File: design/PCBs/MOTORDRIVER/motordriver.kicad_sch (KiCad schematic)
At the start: 0 parts

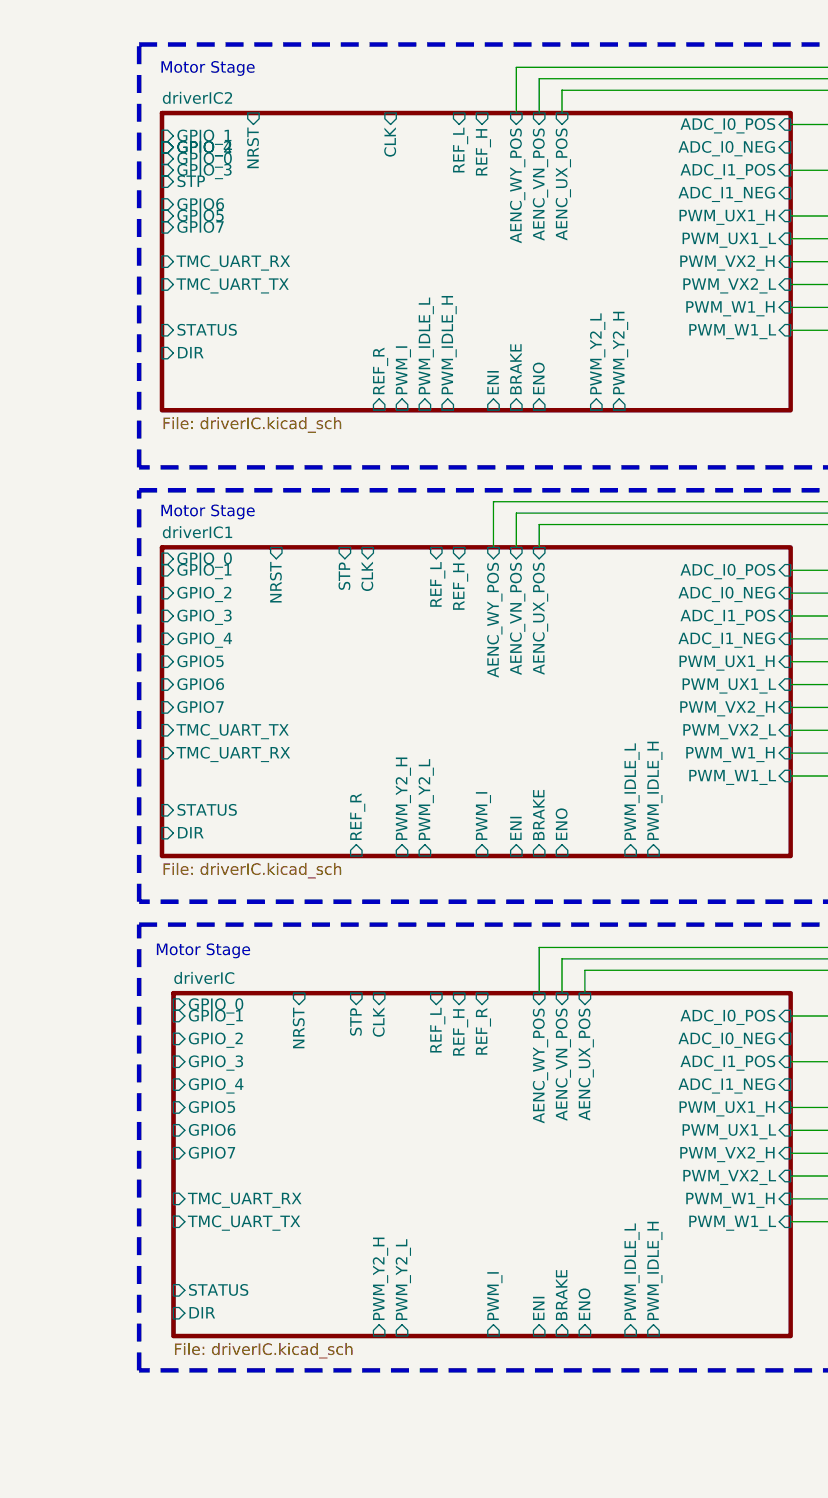
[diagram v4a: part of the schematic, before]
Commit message: Removed unneccessary TMC4761 pins
Finally went through every pin on the TMC and tried to eliminate
unneeded pins. Reduced sheet complexity quite nicely. Pretty much
all rationales for removing pins were added to the design document,
although not formatted that nicely yet.
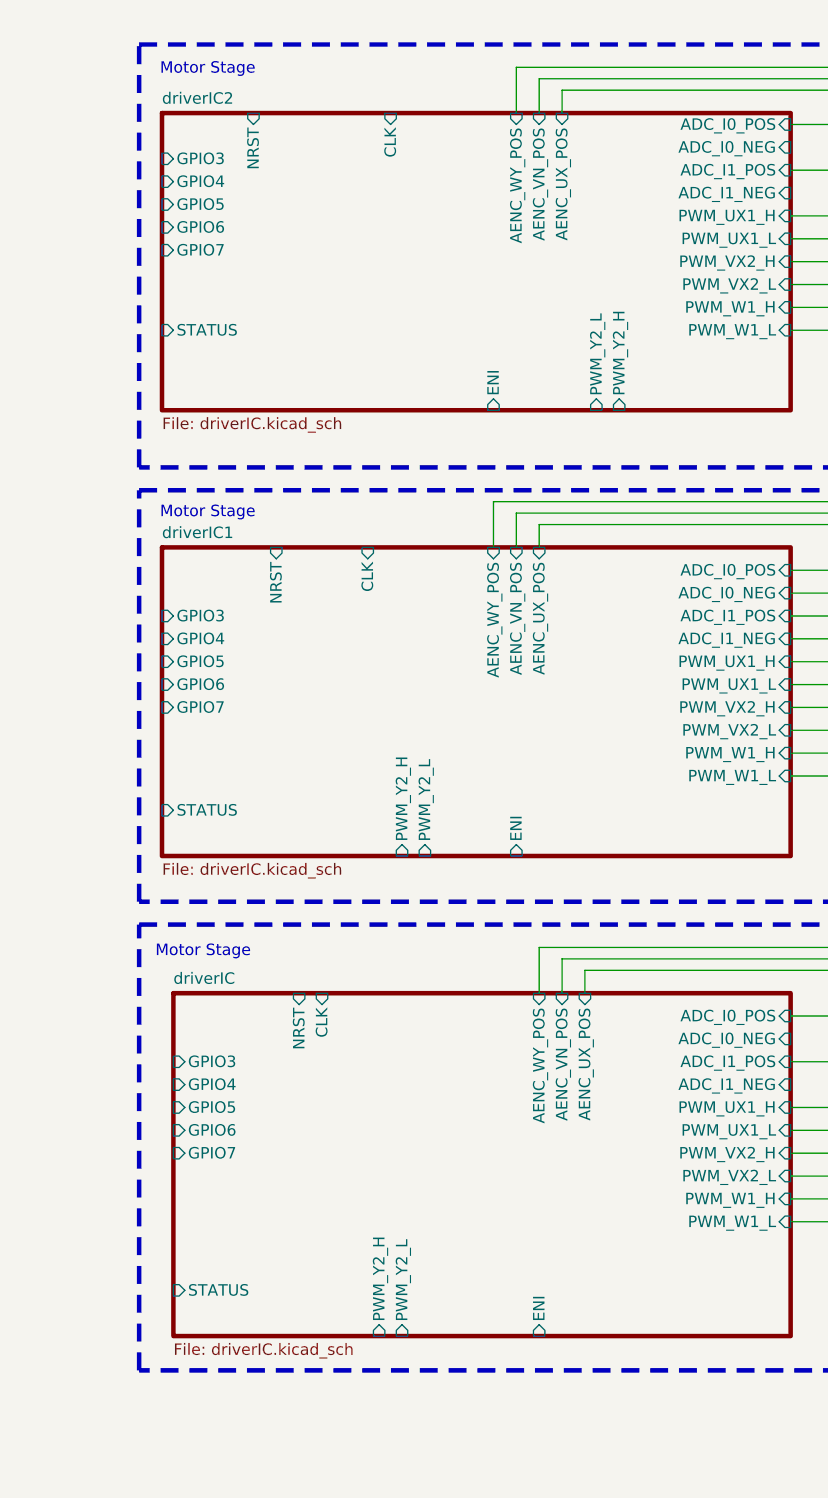
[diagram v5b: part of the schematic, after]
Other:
- sheet driverIC ports: added GPIO3, GPIO4; removed BRAKE, DIR, ENO, GPIO_0, GPIO_1, GPIO_2, GPIO_3, GPIO_4, PWM_I, PWM_IDLE_H, PWM_IDLE_L, REF_H, REF_L, REF_R, STP, TMC_UART_RX, TMC_UART_TX
- sheet driverIC1 ports: added GPIO3, GPIO4; removed BRAKE, DIR, ENO, GPIO_0, GPIO_1, GPIO_2, GPIO_3, GPIO_4, PWM_I, PWM_IDLE_H, PWM_IDLE_L, REF_H, REF_L, REF_R, STP, TMC_UART_RX, TMC_UART_TX
- sheet driverIC2 ports: added GPIO3, GPIO4; removed BRAKE, DIR, ENO, GPIO_0, GPIO_1, GPIO_2, GPIO_3, GPIO_4, PWM_I, PWM_IDLE_H, PWM_IDLE_L, REF_H, REF_L, REF_R, STP, TMC_UART_RX, TMC_UART_TX

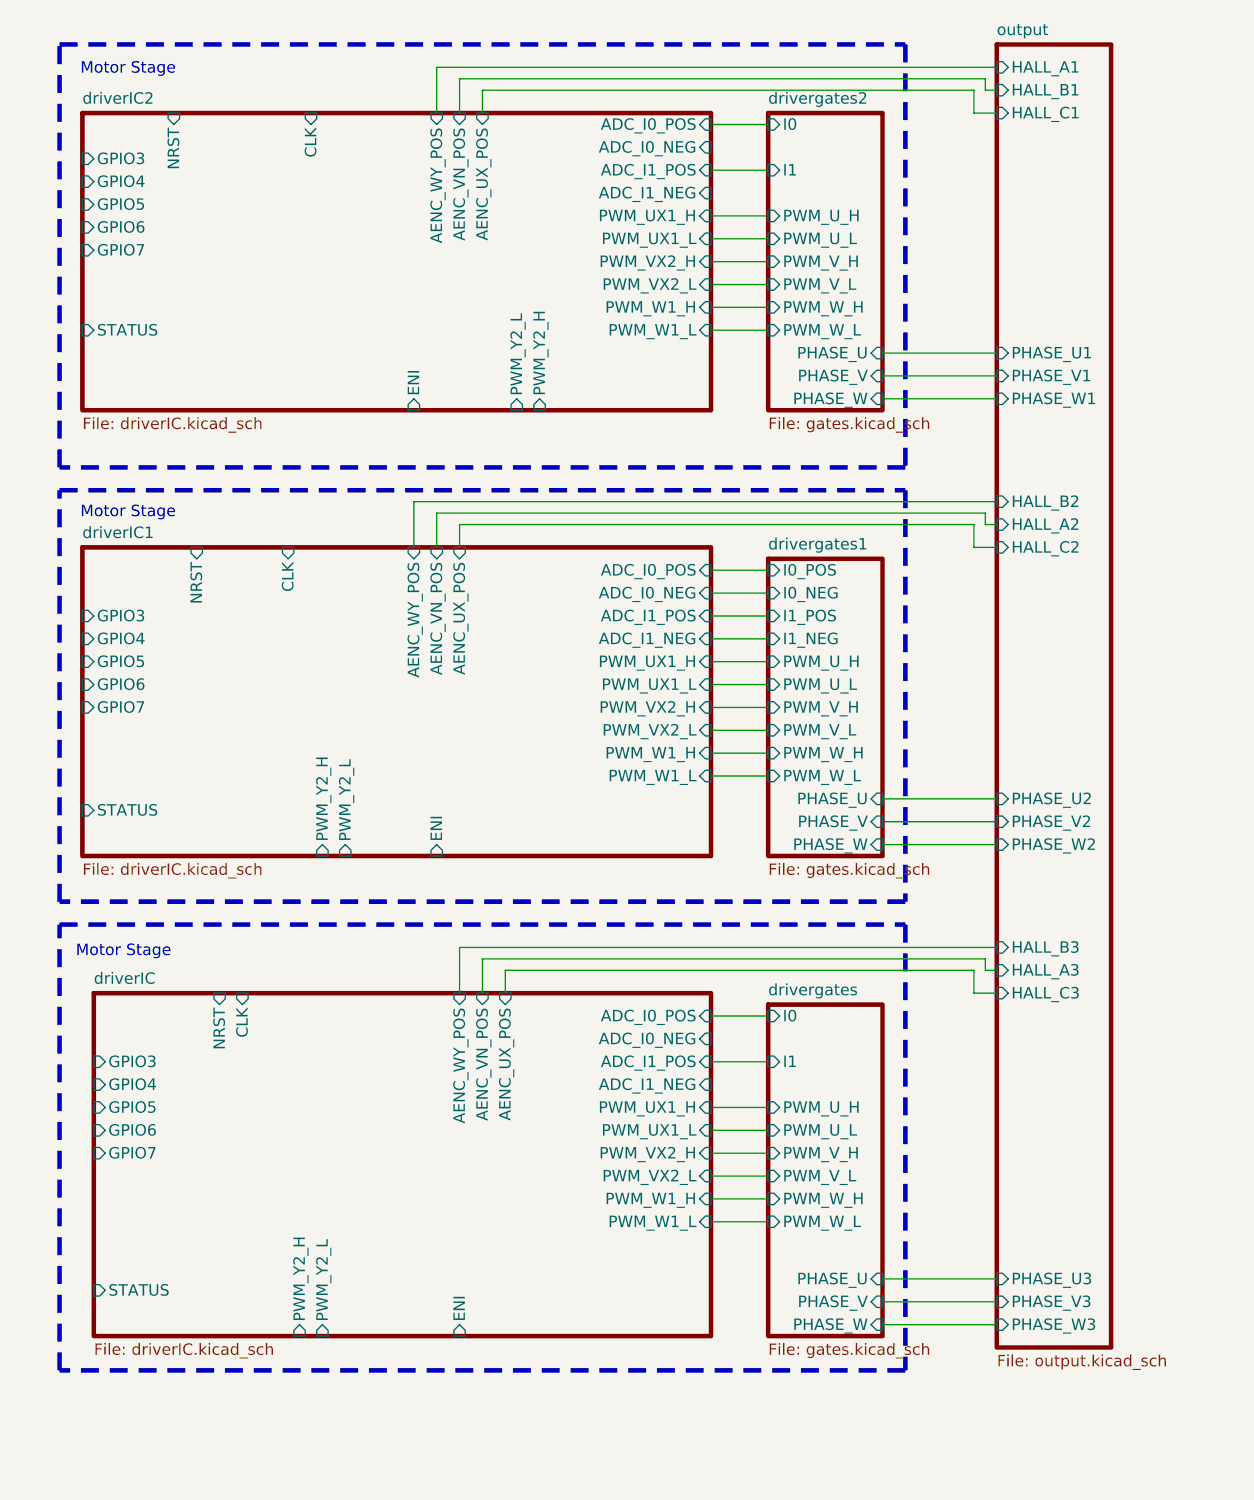
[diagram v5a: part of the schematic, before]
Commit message: Switched TMC hall sensor input to digital from motors
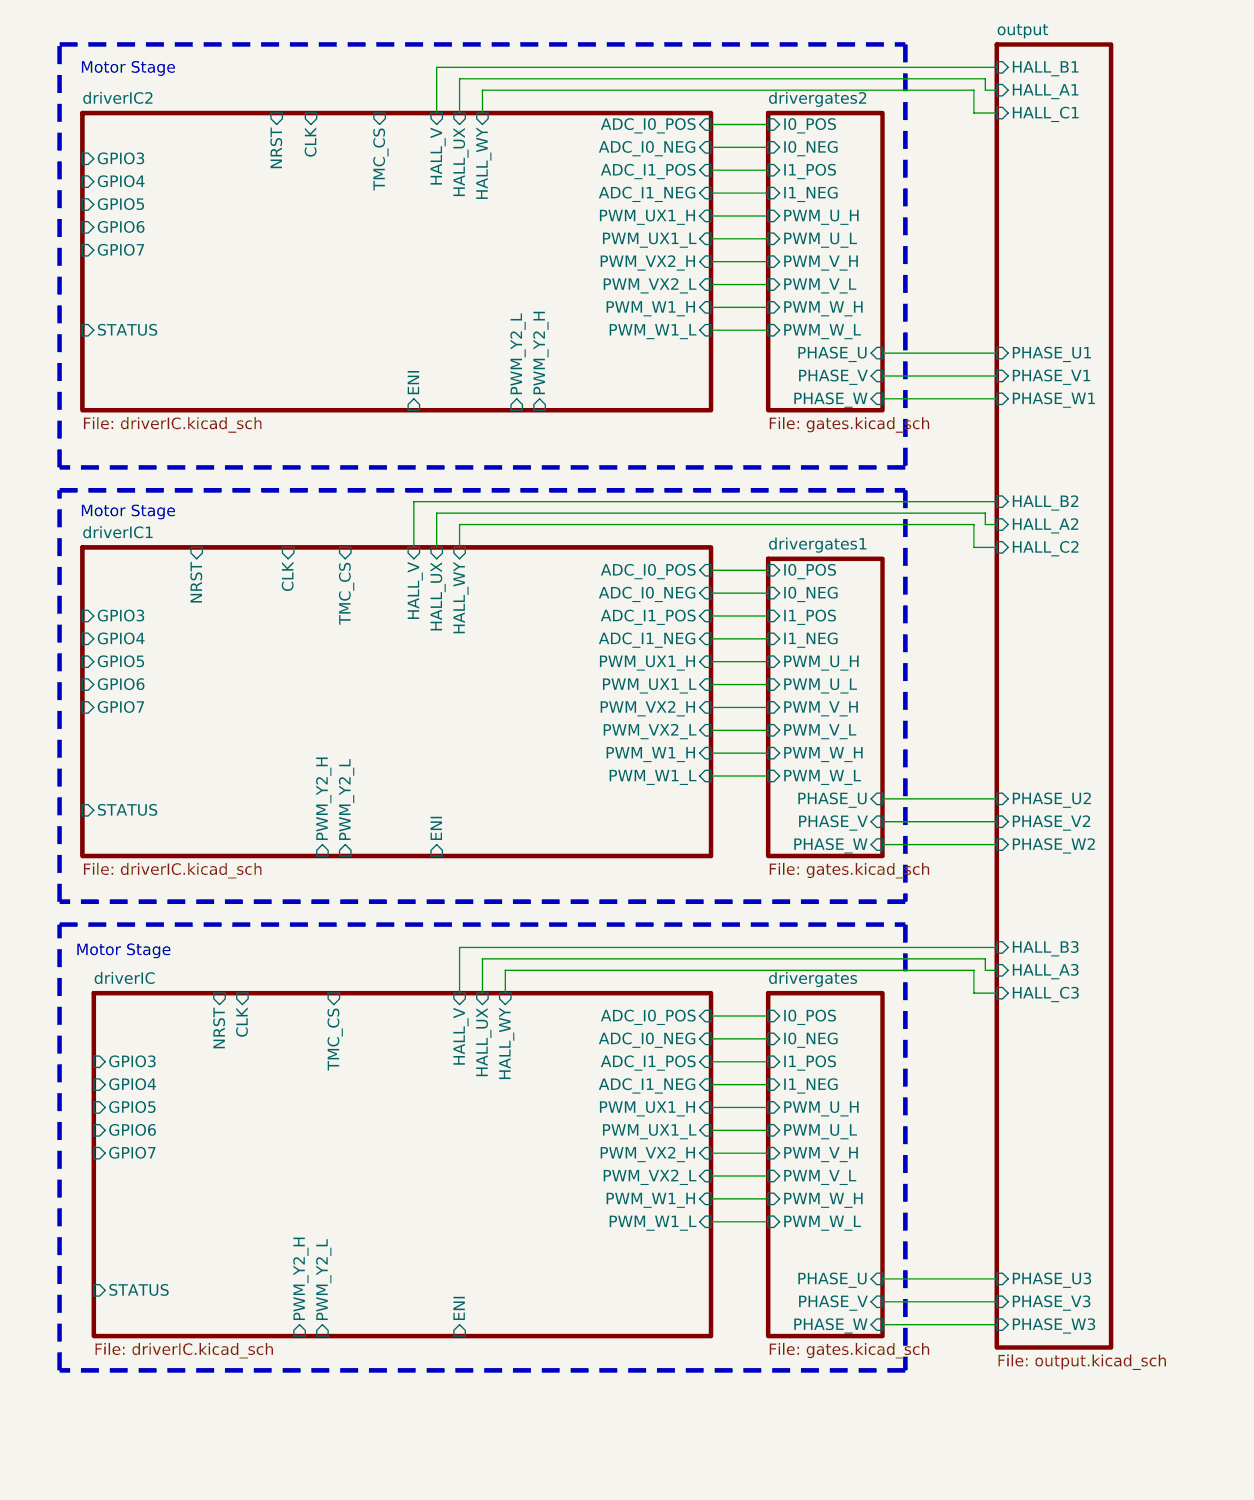
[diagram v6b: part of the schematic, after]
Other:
- sheet driverIC ports: added HALL_UX, HALL_V, HALL_WY, TMC_CS; removed AENC_UX_POS, AENC_VN_POS, AENC_WY_POS
- sheet driverIC1 ports: added HALL_UX, HALL_V, HALL_WY, TMC_CS; removed AENC_UX_POS, AENC_VN_POS, AENC_WY_POS
- sheet driverIC2 ports: added HALL_UX, HALL_V, HALL_WY, TMC_CS; removed AENC_UX_POS, AENC_VN_POS, AENC_WY_POS
- sheet drivergates ports: added I0_NEG, I0_POS, I1_NEG, I1_POS; removed I0, I1
- sheet drivergates2 ports: added I0_NEG, I0_POS, I1_NEG, I1_POS; removed I0, I1

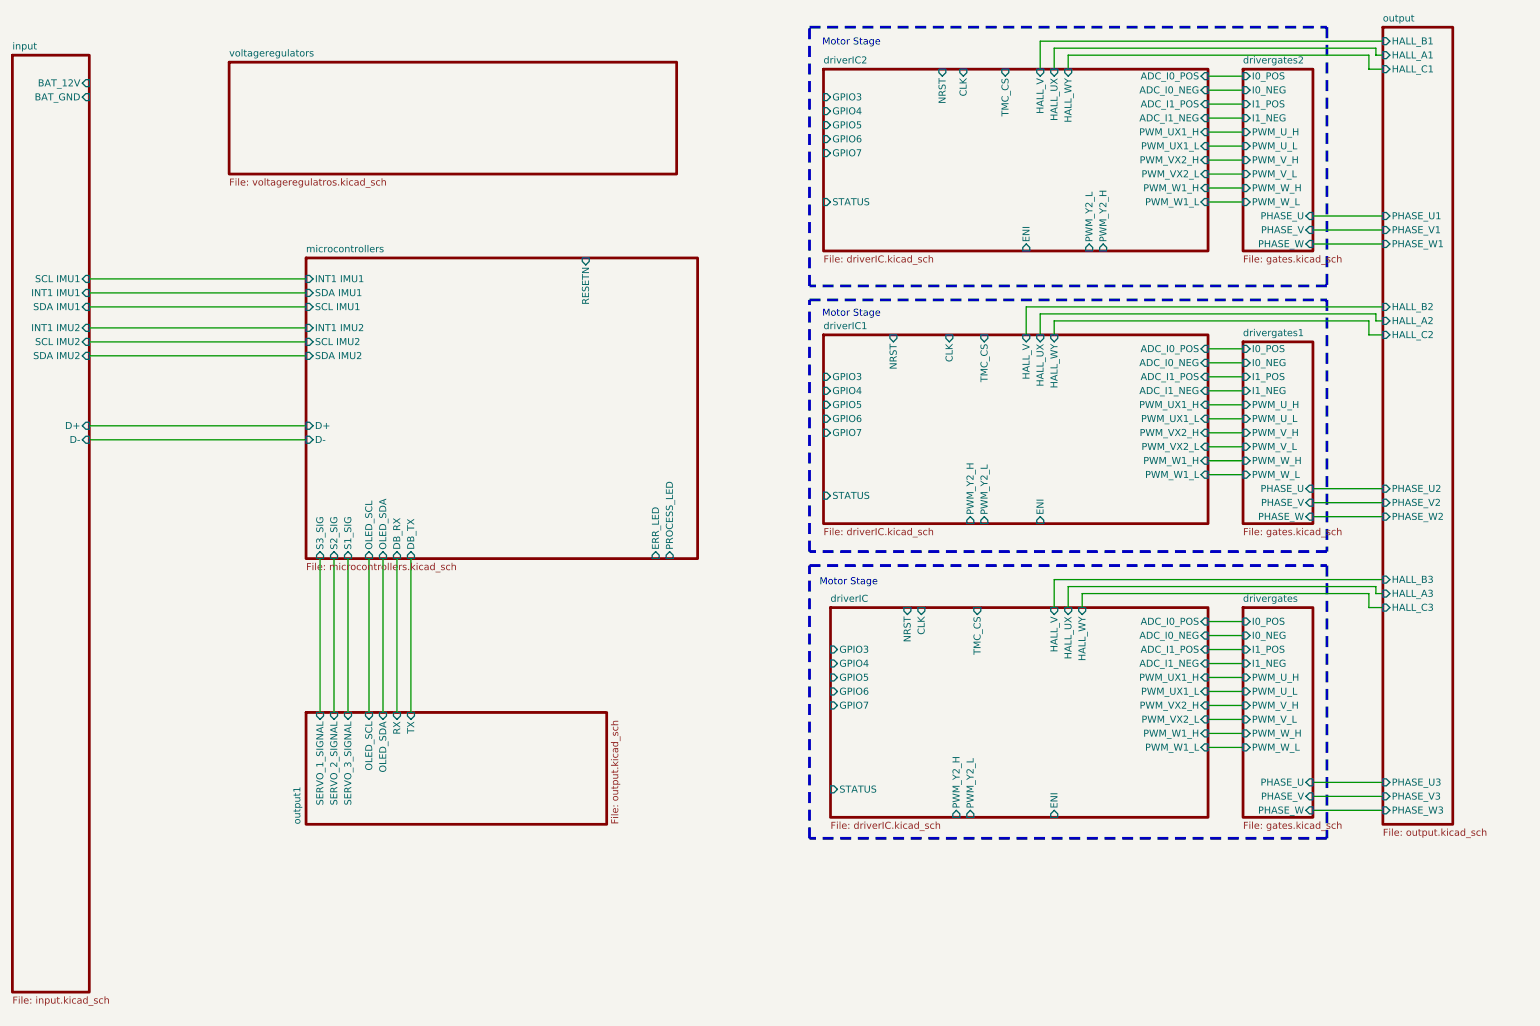
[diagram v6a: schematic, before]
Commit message: TMC and MCU connections
Further progress on PCB. Main remainders are:

Voltage regulator page  (couple todos)
Fix sheet duplication for output sheets
Decide on UART or SPI debug for TMC
Formalize stuff, fill out bottom right on sheets
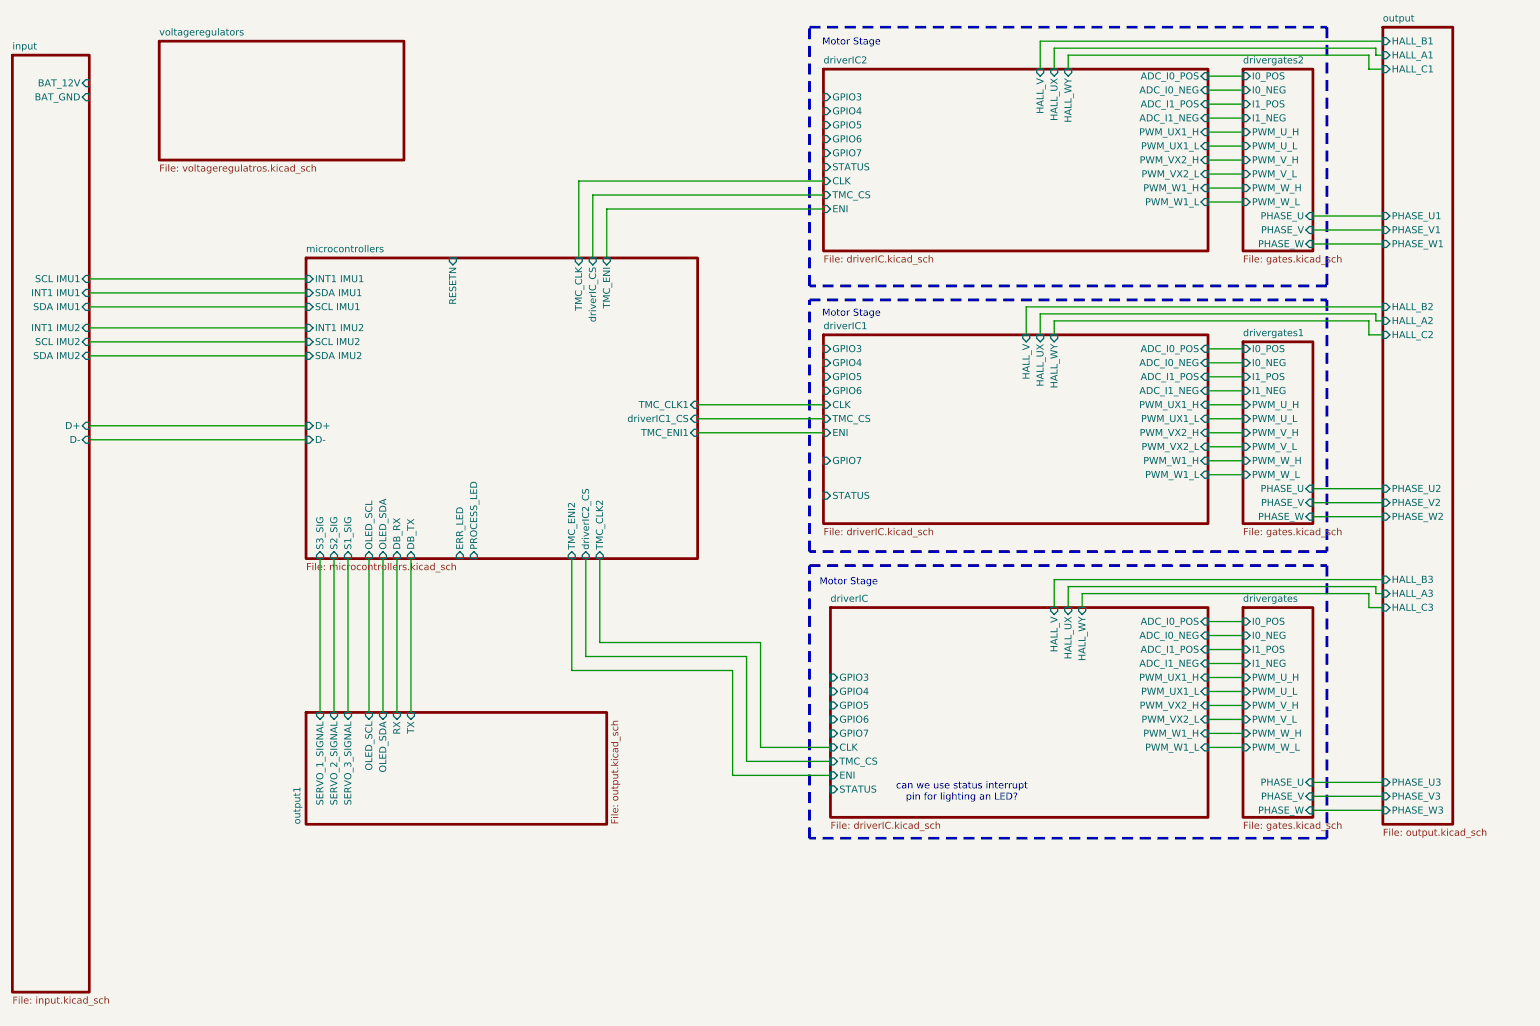
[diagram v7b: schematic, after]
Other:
- sheet driverIC ports: added none; removed NRST, PWM_Y2_H, PWM_Y2_L
- sheet driverIC1 ports: added none; removed NRST, PWM_Y2_H, PWM_Y2_L
- sheet driverIC2 ports: added none; removed NRST, PWM_Y2_H, PWM_Y2_L
- sheet microcontrollers ports: added TMC_CLK, TMC_CLK1, TMC_CLK2, TMC_ENI, TMC_ENI1, TMC_ENI2, driverIC1_CS, driverIC2_CS, driverIC_CS; removed none
- note added: "can we use status interrupt pin for lighting an LED?"
